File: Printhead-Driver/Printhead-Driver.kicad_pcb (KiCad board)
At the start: 4 copper layers, 93.8 x 73 mm, 100 parts, among them J1 IDC_Connector, J2 2 x 10 Pinheader, J3 24V Power In, J4 ADC Select1, U1 TMI8870B, U10 MC34063AD, U11 ADC121C021CIMM, U2 TMI8870B, U3 TMI8870B, U4 TMI8870B, U5 TMI8870B, U6 TMI8870B, U7 TMI8870B, U8 TMI8870B, U9 MCA1101-5-3

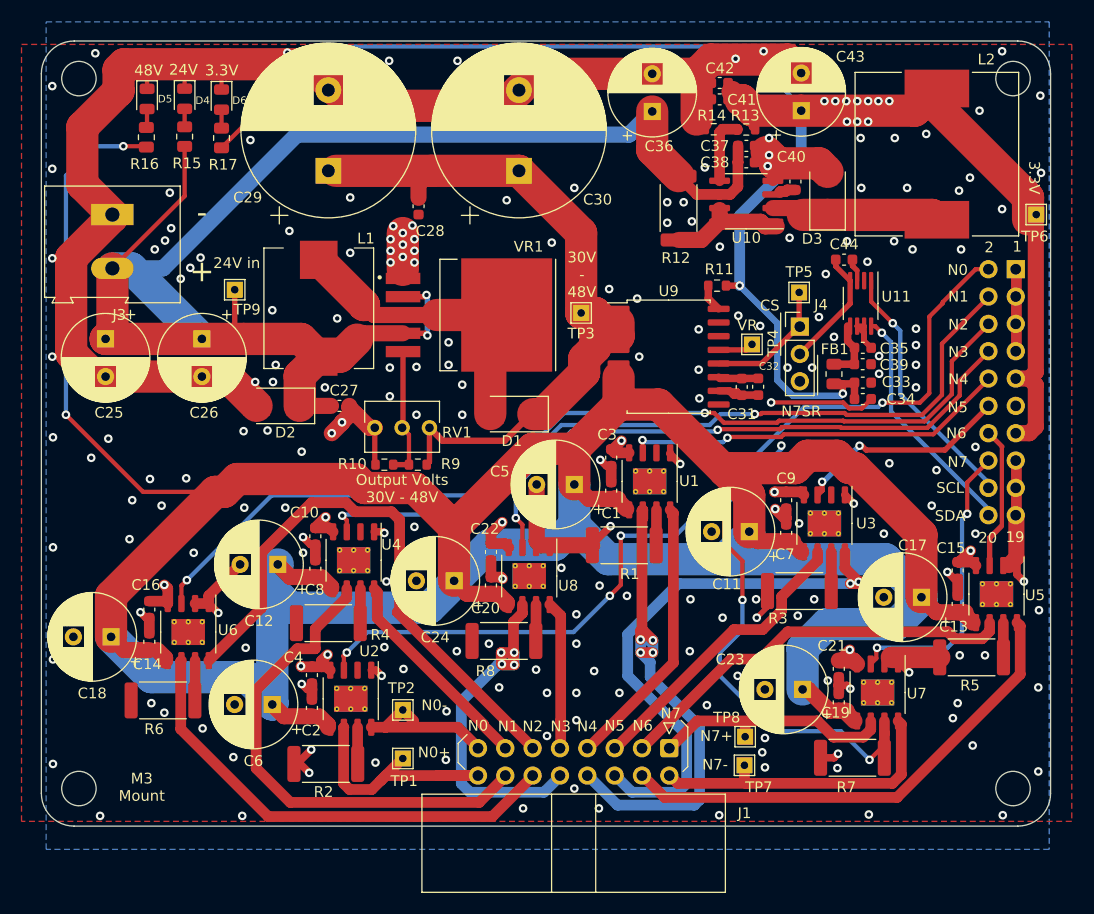
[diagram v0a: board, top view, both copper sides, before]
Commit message: final PCB KiCAD design files for V0.5 as sent off for manufacture at JLCPCB 2022-03-22
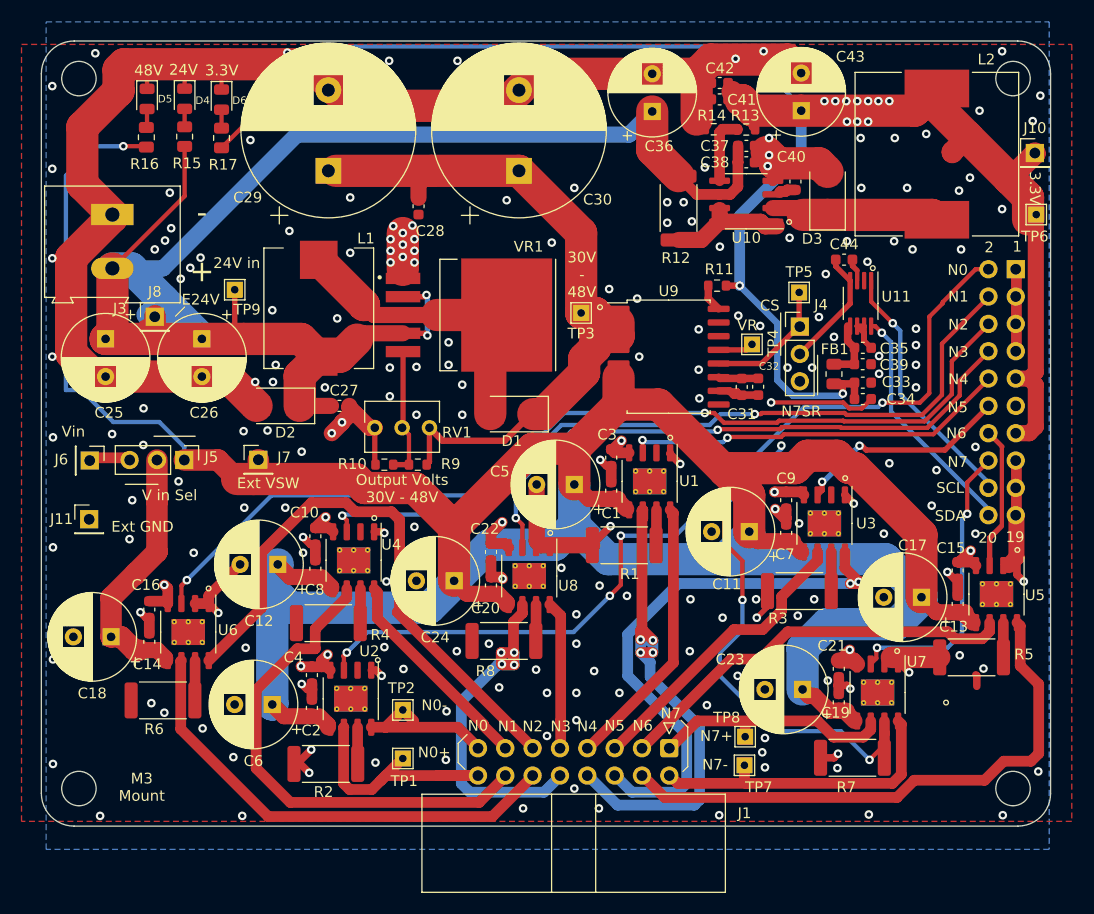
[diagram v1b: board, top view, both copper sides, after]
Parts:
- added J10: External_3.3V, Connector_PinHeader_2.54mm:PinHeader_1x01_P2.54mm_Vertical, F.Cu at (193.3, 72.5)
- added J11: External_GND, Connector_PinHeader_2.54mm:PinHeader_1x01_P2.54mm_Vertical, F.Cu at (105.4, 106.6)
- added J5: Noz2 Voltage Selection, Connector_PinHeader_2.54mm:PinHeader_1x03_P2.54mm_Vertical, F.Cu at (114.2, 101.0)
- added J6: Ext, Connector_PinHeader_2.54mm:PinHeader_1x01_P2.54mm_Vertical, F.Cu at (105.5, 101.1)
- added J7: External_VSW, Connector_PinHeader_2.54mm:PinHeader_1x01_P2.54mm_Vertical, F.Cu at (121.1, 101.0)
- added J8: External_24V, Connector_PinHeader_2.54mm:PinHeader_1x01_P2.54mm_Vertical, F.Cu at (111.5, 87.7)
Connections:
- C14 pad 2: +VSW -> Net-(C14-Pad2)
- C18 pad 1: +VSW -> Net-(C14-Pad2)
- U6 pad 5: +VSW -> Net-(C14-Pad2)
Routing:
- net +VSW: track 343.3 -> 300.4 mm, vias 2 -> 1
- net Net-(C14-Pad2): track 0.00 -> 27.0 mm
- net N6-: track 45.6 -> 52.3 mm
- net +3V3: track 191.8 -> 197.2 mm
- net +24V: track 156.3 -> 160.9 mm
- net Net-(J5-Pad3): track 0.00 -> 3.65 mm
- net GND: track 252.2 -> 253.3 mm, vias 202 -> 196
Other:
- board text added: "E24V"
- board text added: "Ext GND"
- board text added: "Ext VSW"
- board text added: "V in Sel"
- board text added: "Vin"

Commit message: Updating Controller and Driver boards to version 0.6
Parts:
- removed the C1 at (153.9, 103.9)
- removed the C10 at (126.4, 108.1)
- removed the C19 at (175.1, 123.6)
- removed the C2 at (126.1, 124.1)
- removed the C20 at (142.7, 112.7)
- removed the C39 at (177.3, 92.1)
- removed the C43 at (171.6, 68.6)
- removed the D2 at (123.0, 96.0)
- removed FB1: 120uH, Resistor_SMD:R_0805_2012Metric
- removed J10: External_3.3V, Connector_PinHeader_2.54mm:PinHeader_1x01_P2.54mm_Vertical
- removed J11: External_GND, Connector_PinHeader_2.54mm:PinHeader_1x01_P2.54mm_Vertical
- removed J4: ADC Select1, Connector_PinHeader_2.54mm:PinHeader_1x03_P2.54mm_Vertical
- removed J5: Noz2 Voltage Selection, Connector_PinHeader_2.54mm:PinHeader_1x03_P2.54mm_Vertical
- removed J6: Ext, Connector_PinHeader_2.54mm:PinHeader_1x01_P2.54mm_Vertical
- removed J7: External_VSW, Connector_PinHeader_2.54mm:PinHeader_1x01_P2.54mm_Vertical
- removed J8: External_24V, Connector_PinHeader_2.54mm:PinHeader_1x01_P2.54mm_Vertical
- removed the R15 at (114.3, 71.0)
- removed the TP3 at (151.1, 87.4)
- removed the TP4 at (167.0, 90.3)
- removed the U9 at (159.3, 91.4)
- added C12: 100nF, Capacitor_SMD:C_0603_1608Metric, F.Cu at (123.9, 102.0)
- added C15: 100nF, Capacitor_SMD:C_0603_1608Metric, F.Cu at (169.5, 114.6)
- added C16: 100nF, Capacitor_SMD:C_0603_1608Metric, F.Cu at (123.6, 111.2)
- added C21: 1nF**, Capacitor_SMD:C_0603_1608Metric, F.Cu at (190.0, 125.0)
- added C22: 1nF**, Capacitor_SMD:C_0603_1608Metric, F.Cu at (112.9, 123.6)
- added C23: 100nF, Capacitor_SMD:C_0603_1608Metric, F.Cu at (183.9, 125.0)
- added C24: 100nF, Capacitor_SMD:C_0603_1608Metric, F.Cu at (106.7, 124.3)
- added C29: 1nF**, Capacitor_SMD:C_0603_1608Metric, F.Cu at (180.8, 129.5)
- added C36: 100nF, Capacitor_SMD:C_0603_1608Metric, F.Cu at (166.1, 85.5)
- added C37: 100nF, Capacitor_SMD:C_0603_1608Metric, F.Cu at (176.3, 91.1)
- added C38: 1nF/DNF, Capacitor_SMD:C_0603_1608Metric, F.Cu at (165.6, 88.9)
- added C45: 1nF/DNF, Capacitor_SMD:C_0603_1608Metric, F.Cu at (165.1, 93.0)
- added C46: 1nF/DNF, Capacitor_SMD:C_0603_1608Metric, F.Cu at (175.6, 94.4)
- added C47: 1nF/DNF, Capacitor_SMD:C_0603_1608Metric, F.Cu at (178.7, 93.3)
- added C48: 1nF/DNF, Capacitor_SMD:C_0603_1608Metric, F.Cu at (161.5, 91.8)
- added C49: 1nF/DNF, Capacitor_SMD:C_0603_1608Metric, F.Cu at (166.3, 94.6)
- added C5: 1nF**, Capacitor_SMD:C_0603_1608Metric, F.Cu at (159.1, 111.4)
- added C50: 1nF/DNF, Capacitor_SMD:C_0603_1608Metric, F.Cu at (171.3, 95.3)
- added C51: 100nF, Capacitor_SMD:C_0603_1608Metric, F.Cu at (183.7, 82.7)
- added C52: 10uF, Capacitor_SMD:C_0603_1608Metric, F.Cu at (182.2, 82.7)
- added C53: 100nF, Capacitor_SMD:C_0603_1608Metric, F.Cu at (182.9, 79.8)
- added C54: 10uF, Capacitor_SMD:C_0603_1608Metric, F.Cu at (182.9, 78.3)
- added C55: 100nF, Capacitor_SMD:C_0603_1608Metric, F.Cu at (186.0, 75.1)
- added C56: 10uF, Capacitor_SMD:C_0603_1608Metric, F.Cu at (186.0, 73.6)
- added C6: 1nF**DNF, Capacitor_SMD:C_0603_1608Metric, F.Cu at (132.9, 128.5)
- added C61: 100nF 10V, Capacitor_SMD:C_0603_1608Metric, F.Cu at (183.7, 74.4)
- added C64: 100uF/63V, Capacitor_THT:CP_Radial_D8.0mm_P3.50mm, F.Cu at (184.1, 70.3)
- added C65: 100nF, Capacitor_SMD:C_0603_1608Metric, F.Cu at (191.1, 79.0)
- added C66: 10uF, Capacitor_SMD:C_0603_1608Metric, F.Cu at (191.1, 77.4)
- added C67: 100nF, Capacitor_SMD:C_0603_1608Metric, F.Cu at (191.7, 70.3)
- added C68: 1uF, Capacitor_SMD:C_0603_1608Metric, F.Cu at (191.7, 71.8)
- added D3: 12V, Diode_SMD:D_0805_2012Metric, F.Cu at (119.8, 86.5)
- added D6: Green, Diode_SMD:D_0603_1608Metric, F.Cu at (117.7, 67.5)
- added F1: 5A, Pauls_KiCAD_Libraries:Fuse_Holder_1808_10.0mmx5mm, F.Cu at (118.9, 76.6)
- added L1: 1uH 1.4A, Inductor_SMD:L_0805_2012Metric, F.Cu at (169.2, 85.2)
- added L3: 1uH 4A, Inductor_SMD:L_Taiyo-Yuden_MD-5050, F.Cu at (153.2, 91.2)
- added L4: 1uH 1.4A, Inductor_SMD:L_0805_2012Metric, F.Cu at (185.3, 82.9)
- added L6: 1uH/1.4A, Inductor_SMD:L_0805_2012Metric, F.Cu at (181.5, 74.5)
- added Q1: RU30L30, Pauls_KiCAD_Libraries:PDFN3333, F.Cu at (116.6, 84.2)
- added R16: 27K, Resistor_SMD:R_0603_1608Metric, F.Cu at (114.3, 70.4)
- added R18: 4.7K, Resistor_SMD:R_0603_1608Metric, F.Cu at (117.7, 70.5)
- added R20: 100k, Resistor_SMD:R_0603_1608Metric, F.Cu at (119.7, 83.2)
- added R9: 88K, Resistor_SMD:R_0603_1608Metric, F.Cu at (158.7, 85.9)
- added TP10: TestPoint, TestPoint:TestPoint_THTPad_1.5x1.5mm_Drill0.7mm, F.Cu at (102.5, 114.3)
- added TP6: TestPoint, TestPoint:TestPoint_THTPad_1.5x1.5mm_Drill0.7mm, F.Cu at (179.2, 86.2)
- added TP8: TestPoint, TestPoint:TestPoint_THTPad_1.5x1.5mm_Drill0.7mm, F.Cu at (193.5, 99.6)
- added U12: INA180, Package_TO_SOT_SMD:SOT-23-5, F.Cu at (109.8, 126.3)
- added U15: INA180, Package_TO_SOT_SMD:SOT-23-5, F.Cu at (177.8, 131.5)
- added U16: INA180, Package_TO_SOT_SMD:SOT-23-5, F.Cu at (145.8, 120.8)
- added U17: ADC128S102CIMTX, Package_SO:TSSOP-16_4.4x5mm_P0.65mm, F.Cu at (171.2, 90.9)
- added U18: HE6550MPR, Package_TO_SOT_SMD:SOT-89-3, F.Cu at (187.0, 78.4)
- added U20: XC6227C331MR, Package_TO_SOT_SMD:SOT-23-5, F.Cu at (191.4, 74.5)
- added U3: INA180, Package_TO_SOT_SMD:SOT-23-5, F.Cu at (156.6, 111.9)
- added U6: TMI8870B, Package_SO:HSOP-8-1EP_3.9x4.9mm_P1.27mm_EP2.41x3.1mm_ThermalVias, F.Cu at (127.5, 104.3)
- added U7: INA180, Package_TO_SOT_SMD:SOT-23-5, F.Cu at (172.8, 115.8)
- added U8: INA180, Package_TO_SOT_SMD:SOT-23-5, F.Cu at (126.8, 113.1)
- C13, C14: value 100nF -> 1nF**
- C30: value 1000uF/63V -> 1nF**; footprint Capacitor_THT:CP_Radial_D16.0mm_P7.50mm -> Capacitor_SMD:C_0603_1608Metric
- C32: value 22uF -> 100nF
- C33: value 10uF -> 1uF
- C35: value 4.7uF -> 1uF
- C41: renamed from C27; value 100nF/50V -> 100nF/100V
- C44: value 100nF-DNF -> 1nF/DNF
- C58: renamed from C37; value 22uF/50V -> 22uF/35V; footprint Capacitor_SMD:C_0603_1608Metric -> Capacitor_SMD:C_1210_3225Metric
- C59: renamed from C38; value 100nF/50V -> 100nF/35V; footprint Capacitor_SMD:C_0603_1608Metric -> Capacitor_SMD:C_1206_3216Metric
- C62: renamed from C41; value 100nF -> 100nF 10V
- C8: value 100nF -> 100nF-DNF
- D4, D5: footprint LED_SMD:LED_0805_2012Metric -> Diode_SMD:D_0603_1608Metric
- D7: renamed from D6; footprint LED_SMD:LED_0805_2012Metric -> Diode_SMD:D_0603_1608Metric
- J2: value 2 x 10 Pinheader -> Controller; footprint Connector_PinHeader_2.54mm:PinHeader_2x10_P2.54mm_Vertical -> Connector_PinHeader_2.54mm:PinHeader_2x12_P2.54mm_Vertical
- J3: footprint TerminalBlock:TerminalBlock_Altech_AK300-2_P5.00mm -> Pauls_KiCAD_Libraries:JST-XH-2P_SMD
- R1, R2, R3, R4, R5, R6, R7, R8: footprint Resistor_SMD:R_2512_6332Metric -> Resistor_SMD:R_1206_3216Metric
- R10: renamed from R9; value 10K -> 10K-DNF
- R11: value 10K -> 12K
- R12: renamed from R10; value 10K -> 10K-DNF
- R13: renamed from R12; footprint Resistor_SMD:R_2512_6332Metric -> Resistor_SMD:R_1206_3216Metric
- R14: renamed from R13; value 3K -> 4.7K
- R15: renamed from R14; value 1.8K -> 1.3K
- R17: renamed from R16; value 60K -> 62K; footprint Resistor_SMD:R_0805_2012Metric -> Resistor_SMD:R_0603_1608Metric
- R19: renamed from R17; footprint Resistor_SMD:R_0805_2012Metric -> Resistor_SMD:R_0603_1608Metric
- U11: value ADC121C021CIMM -> INA180; footprint Package_SO:MSOP-8_3x3mm_P0.65mm -> Package_TO_SOT_SMD:SOT-23-5
- U4: value TMI8870B -> INA180-DNF; footprint Package_SO:HSOP-8-1EP_3.9x4.9mm_P1.27mm_EP2.41x3.1mm_ThermalVias -> Package_TO_SOT_SMD:SOT-23-5
- moved C30 44.0 mm to (148.4, 118.1)
- moved U11 41.9 mm to (187.1, 127.2), turned to 90 degrees
- moved C31 37.0 mm to (174.5, 130.3), turned to 180 degrees
- moved TP7 36.6 mm to (159.4, 64.8)
- moved C32 35.7 mm to (142.3, 119.4), turned to 90 degrees
- moved U4 20.2 mm to (129.7, 130.6), turned to 90 degrees
- moved C14 20.0 mm to (129.8, 111.0), turned to 90 degrees
- moved C8 18.3 mm to (126.4, 129.4), turned to 180 degrees
- moved C7 17.2 mm to (153.2, 110.8), turned to 180 degrees
- moved TP5 17.2 mm to (154.2, 86.7), turned to 0 degrees
- moved C44 14.8 mm to (163.1, 90.3), turned to 180 degrees
- moved TP9 14.3 mm to (110.3, 73.9)
- moved L5 12.3 mm to (171.9, 72.4)
- moved C58 12.1 mm to (154.5, 70.1)
- moved C59 12.0 mm to (154.5, 72.9)
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- renumbered C5 to C1, C12 to C10, C9 to C11, C15 to C19, C6 to C2, C16 to C20, C23 to C25, C24 to C26, C21 to C27, C22 to C28, C25 to C39, C26 to C40, C28 to C42, C29 to C43, C36 to C57, C40 to C60, C42 to C63, C11 to C9, D3 to D2, L1 to L2, L2 to L5, TP7 to TP3, TP8 to TP4, TP6 to TP7, U6 to U10, U7 to U13, U8 to U14, U10 to U19, U3 to U5, U5 to U9
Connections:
- net NOZ7SR renamed Net-(C29-Pad2)
- C13 pad 2: +VSW -> Net-(C13-Pad2)
- C18 pad 1: Net-(C14-Pad2) -> +VSW
- C30 pad 1: Net-(C28-Pad1) -> GND
- C30 pad 2: GND -> Net-(C30-Pad2)
- C31 pad 1: Net-(C31-Pad1) -> +5V
- C32 pad 1: GND -> +5V
- C32 pad 2: Net-(C31-Pad1) -> GND
- C33 pad 1: GND -> +5V
- C33 pad 2: +3V3 -> GND
- C34 pad 1: GND -> +5V
- C34 pad 2: +3V3 -> GND
- C35 pad 1: GND -> Net-(C35-Pad1)
- C35 pad 2: Net-(C35-Pad2) -> GND
- C42 pad 1: Net-(C28-Pad1) -> Net-(C42-Pad1)
- C43 pad 1: Net-(C28-Pad1) -> Net-(C42-Pad1)
- C44 pad 1: Net-(C44-Pad1) -> NR1
- C62 pad 1: +3V3 -> Net-(C62-Pad1)
- C63 pad 1: +3V3 -> Net-(C62-Pad1)
- C7 pad 1: GND -> +5V
- C7 pad 2: +VSW -> GND
- C8 pad 1: GND -> +5V
- C8 pad 2: +VSW -> GND
- D1 pad 1: Net-(C28-Pad1) -> Net-(C42-Pad1)
- J2 pad 18: SCL -> SLCK
- J2 pad 20: SDA -> MISO
- J3 pad 2: +24V -> Net-(F1-Pad1)
- L5 pad 1: +3V3 -> Net-(C62-Pad1)
- R10 pad 2: Net-(C28-Pad1) -> Net-(C42-Pad1)
- R11 pad 1: Net-(R11-Pad1) -> GND
- R11 pad 2: +3V3 -> VSW_Divider
- R14 pad 1: +3V3 -> Net-(C62-Pad1)
- R2 pad 2: Net-(R2-Pad2) -> Net-(C6-Pad2)
- R3 pad 2: Net-(R3-Pad2) -> Net-(C13-Pad2)
- R4 pad 2: Net-(R4-Pad2) -> Net-(C14-Pad2)
- R5 pad 2: Net-(R5-Pad2) -> Net-(C21-Pad2)
- R8 pad 2: Net-(R8-Pad2) -> Net-(C30-Pad2)
- RV1 pad 3: Net-(C28-Pad1) -> Net-(C42-Pad1)
- TP5 pad 1: Net-(J4-Pad1) -> +VSW
- TP7 pad 1: +3V3 -> Net-(C62-Pad1)
- TP9 pad 1: +24V -> Net-(F1-Pad1)
- U10 pad 5: Net-(C14-Pad2) -> +VSW
- U11 pad 1: SCL -> NR6
- U11 pad 2: (no net) -> GND
- U11 pad 3: GND -> Net-(C21-Pad2)
- U11 pad 4: Net-(C44-Pad1) -> GND
- U11 pad 5: Net-(C35-Pad2) -> +5V
- U14 pad 7: Net-(R8-Pad2) -> Net-(C30-Pad2)
- U2 pad 7: Net-(R2-Pad2) -> Net-(C6-Pad2)
- U4 pad 1: GND -> (no net)
- U4 pad 3: PH1 -> Net-(C6-Pad2)
- U4 pad 4: +3V3 -> GND
- U4 pad 5: +VSW -> +5V
- U5 pad 7: Net-(R3-Pad2) -> Net-(C13-Pad2)
- U9 pad 7: Net-(R5-Pad2) -> Net-(C21-Pad2)
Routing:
- net +5V: track 0.00 -> 335.9 mm, vias 0 -> 13
- net GND: track 253.3 -> 339.8 mm, vias 196 -> 156
- net NR2: track 0.00 -> 78.1 mm, vias 0 -> 2
- net Net-(C28-Pad1): track 68.3 -> 0.00 mm
- net NR1: track 0.00 -> 57.7 mm, vias 0 -> 2
- net NR7: track 0.00 -> 50.6 mm, vias 0 -> 2
- net Net-(C42-Pad1): track 0.00 -> 49.7 mm
- net NR6: track 0.00 -> 49.0 mm, vias 0 -> 2
- net NR3: track 0.00 -> 47.2 mm, vias 0 -> 2
- net Net-(C29-Pad2): track 55.4 -> 10.3 mm, vias 4 -> 0
- net Net-(C62-Pad1): track 0.00 -> 36.5 mm
- net +3V3: track 197.2 -> 233.3 mm, vias 22 -> 23
- net CS: track 0.00 -> 35.4 mm, vias 0 -> 1
- net +6V: track 0.00 -> 33.8 mm
- net MOSI: track 0.00 -> 29.8 mm, vias 0 -> 1
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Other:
- board text added: "+25V - 44V @ 4A"
- board text added: "+VSW"
- board text added: "23"
- board text added: "24"
- board text added: "24V Vin"
- board text added: "5V"
- board text added: "6V"
- board text added: "MISO"
- board text added: "MOSI"
- board text added: "Output Volts 25V - 45V"
- board text added: "PRL V0.6"
- board text added: "S/N:"
- board text added: "SCLK"
- board text removed: "+30V - 48V @ 1.5A"
- board text removed: "19"
- board text removed: "20"
- board text removed: "24V in"
- board text removed: "30V - 48V"
- board text removed: "E24V"
- board text removed: "Ext GND"
- board text removed: "Ext VSW"
- board text removed: "Hall Effect CurSen"
- board text removed: "N7 Sense Resistor"
- board text removed: "N7SR"
- board text removed: "Output Volts 30V - 48V"
- board text removed: "PRL V10.5"
- board text removed: "SCL"
- board text removed: "SDA"
- board text removed: "V in Sel"
- board text removed: "VR"
- board text removed: "Vin"

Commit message: Adding in version 0.7 KiACD design files
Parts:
- added Q2: RU30L30, Pauls_KiCAD_Libraries:PDFN3333, F.Cu at (110.7, 87.6)
- added R21: 130, Resistor_SMD:R_0603_1608Metric, F.Cu at (168.2, 84.5)
- added R22: 150R, Resistor_SMD:R_0603_1608Metric, F.Cu at (155.7, 65.3)
- added R23: 100*, Resistor_SMD:R_0603_1608Metric, F.Cu at (161.7, 88.0)
- added R24: 100k, Resistor_SMD:R_0603_1608Metric, F.Cu at (110.3, 83.8)
- added SW1: PWR SW C128955, Pauls_KiCAD_Libraries:SW_SMD_SPDT_PCM12_7.8x3.8, F.Cu at (103.5, 89.1)
- added TP11: TestPoint, TestPoint:TestPoint_THTPad_1.5x1.5mm_Drill0.7mm, F.Cu at (160.6, 86.1)
- added TP12: TestPoint, TestPoint:TestPoint_THTPad_1.5x1.5mm_Drill0.7mm, F.Cu at (163.2, 85.9)
- added U21: LM4040DIM3X-5, Package_TO_SOT_SMD:SOT-23, F.Cu at (164.2, 83.9)
- C38: value 1nF/DNF -> 10nF/DNF
- D3: footprint Diode_SMD:D_0805_2012Metric -> Diode_SMD:D_SOD-123
- R11: value 12K -> 10K
- R15: value 1.3K -> 1.0K
- R9: value 88K -> 100K
- moved C39 6.16 mm to (106.8, 95.9)
- moved D3 4.60 mm to (115.5, 88.2), turned to 0 degrees
- moved C40 4.55 mm to (115.5, 94.3)
- moved C62 2.50 mm to (157.4, 65.3)
- moved C63 2.50 mm to (158.9, 65.3)
- moved C33 2.25 mm to (172.9, 84.0)
- moved C34 2.25 mm to (174.4, 84.0)
- moved C35 2.25 mm to (169.6, 84.6)
- moved L1 2.25 mm to (171.3, 84.3)
- moved C18 1.83 mm to (108.7, 109.1)
- moved TP7 1.66 mm to (161.1, 64.7)
- moved Q1 1.61 mm to (115.0, 84.1)
- moved R20 1.22 mm to (118.8, 82.4), turned to 0 degrees
- moved C36 1.13 mm to (166.7, 84.5)
- moved L6 0.79 mm to (180.9, 73.9), turned to 90 degrees
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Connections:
- C33 pad 1: +5V -> +6V
- C34 pad 1: +5V -> +6V
- C36 pad 1: Net-(C35-Pad1) -> Net-(C36-Pad1)
- C38 pad 1: VSW_Divider -> Net-(C38-Pad1)
- D3 pad 1: +24V -> Net-(D3-Pad1)
- L1 pad 2: +5V -> +6V
- Q1 pad 1: +24V -> Net-(D3-Pad1)
- R15 pad 1: Net-(R14-Pad2) -> Net-(R15-Pad1)
- U17 pad 2: Net-(C35-Pad1) -> Net-(C36-Pad1)
- U17 pad 4: VSW_Divider -> Net-(C38-Pad1)
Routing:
- net Net-(D3-Pad2): track 3.84 -> 22.5 mm, vias 0 -> 2
- net +6V: track 33.8 -> 50.3 mm
- net Net-(R24-Pad1): track 0.00 -> 16.0 mm
- net +24V: track 132.6 -> 144.9 mm
- net Net-(C36-Pad1): track 0.00 -> 11.8 mm
- net +5V: track 335.9 -> 325.9 mm
- net Net-(D3-Pad1): track 0.00 -> 9.45 mm
- net Net-(C35-Pad1): track 10.6 -> 3.34 mm
- net Net-(C38-Pad1): track 0.00 -> 7.26 mm
- net VSW_Divider: track 12.4 -> 5.57 mm
- net Net-(Q2-Pad2): track 0.00 -> 6.63 mm
- net GND: track 339.8 -> 342.9 mm
- net Net-(R15-Pad1): track 0.00 -> 2.35 mm
- net +VSW: track 324.1 -> 321.9 mm
- net Net-(C62-Pad1): track 36.5 -> 38.0 mm
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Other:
- board text added: "+5V"
- board text added: "1/10 VSW"
- board text added: "OFF"
- board text added: "ON"
- board text added: "PRL V0.7"
- board text added: "Vd"
- board text added: "Vr"
- board text removed: "PRL V0.6"
